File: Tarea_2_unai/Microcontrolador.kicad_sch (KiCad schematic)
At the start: 6 parts, among them J1 Conn_01x04_Pin, U1 ESP32-C3-DevKitM-1

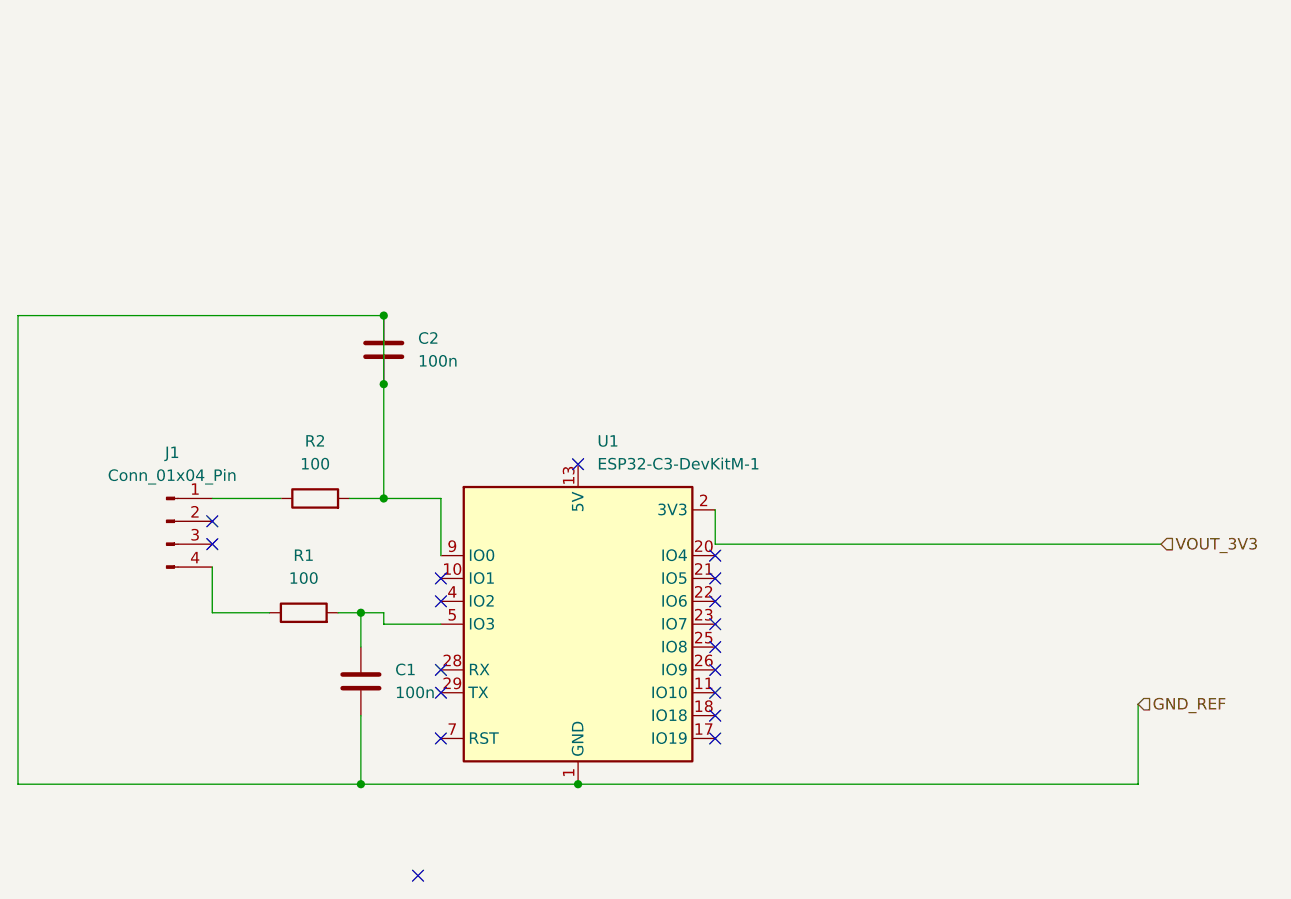
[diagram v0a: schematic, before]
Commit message: cambio de huellas
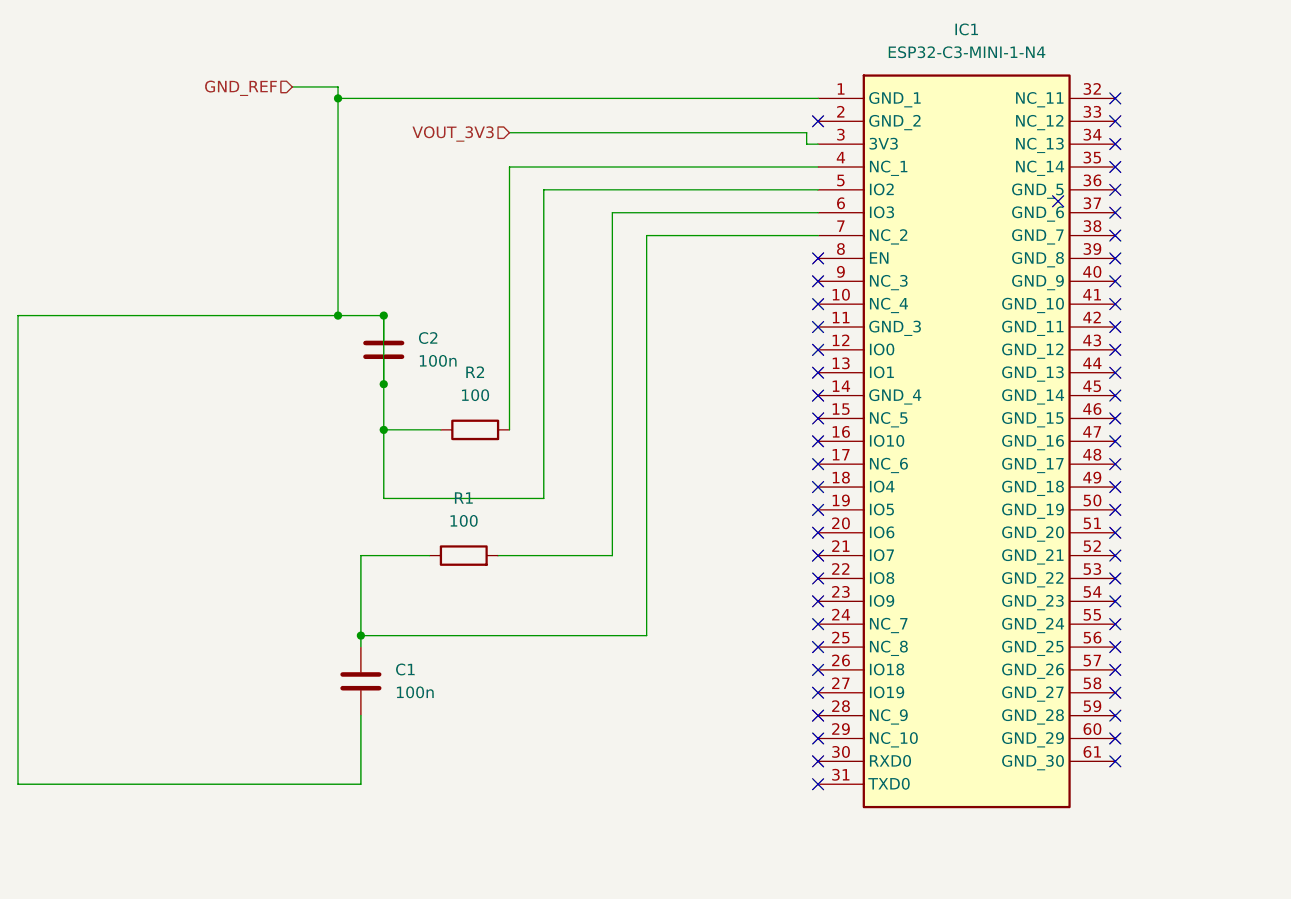
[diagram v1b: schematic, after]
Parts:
- removed J1: Conn_01x04_Pin, RF_Module:ESP32-C3-DevKitM-1, symbol Connector:Conn_01x04_Pin
- removed U1: ESP32-C3-DevKitM-1, RF_Module:ESP32-C3-MINI-1, symbol RF_Module:ESP32-C3-DevKitM-1
- added IC1: ESP32-C3-MINI-1-N4, ESP32C3MINI1N4, symbol ESP32-C3-MINI-1-N4:ESP32-C3-MINI-1-N4
- C1, C2: footprint (none) -> 0201ZK100GBSTR
- R1, R2: footprint (none) -> ERJ-3EKF1000V
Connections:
- net GND_REF: now also R2.1, IC1.1 (GND_1), IC1.5 (IO2); no longer R2.2
- net VOUT_3V3: now also IC1.3 (3V3)
- net at R1.1: now also C1.1, IC1.7 (NC_2)
- net at R1.2: now also IC1.6 (IO3); no longer C1.1
- new net: IC1.4 (NC_1), R2.2
- no-connect marks 18 -> 56
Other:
- moved on the sheet: R1, R2
